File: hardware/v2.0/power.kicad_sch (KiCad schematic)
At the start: 60 parts, among them U1 ECP5U-25F-CABGA256, U2 LTC3407AEDD-2_PBF, U3 TLV62569DBV, U4 LP5912-1.8DRV

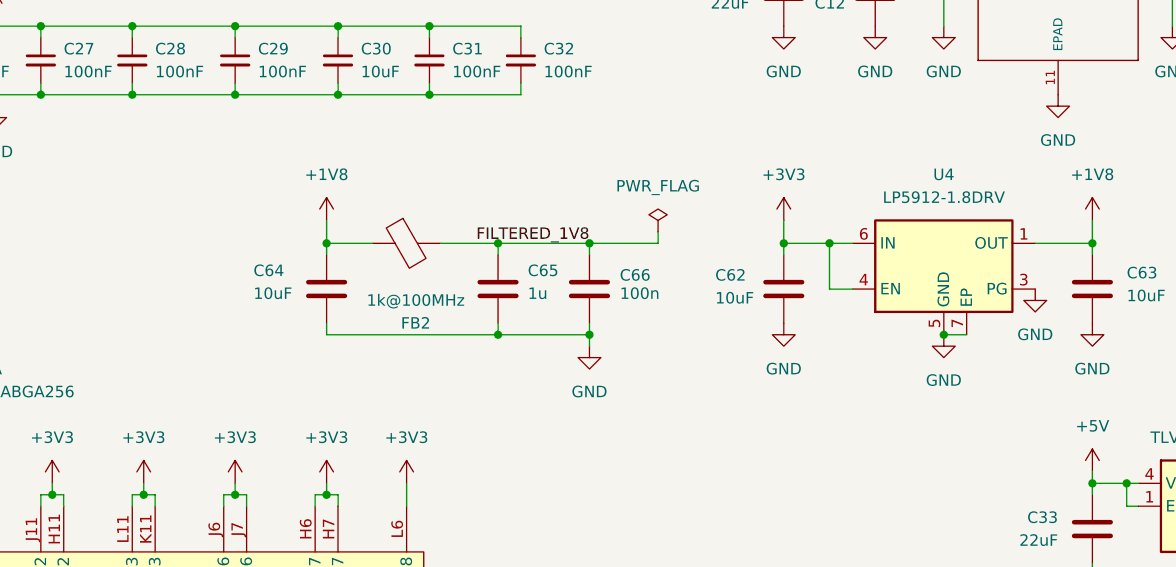
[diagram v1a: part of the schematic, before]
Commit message: ADC driver power and signal input
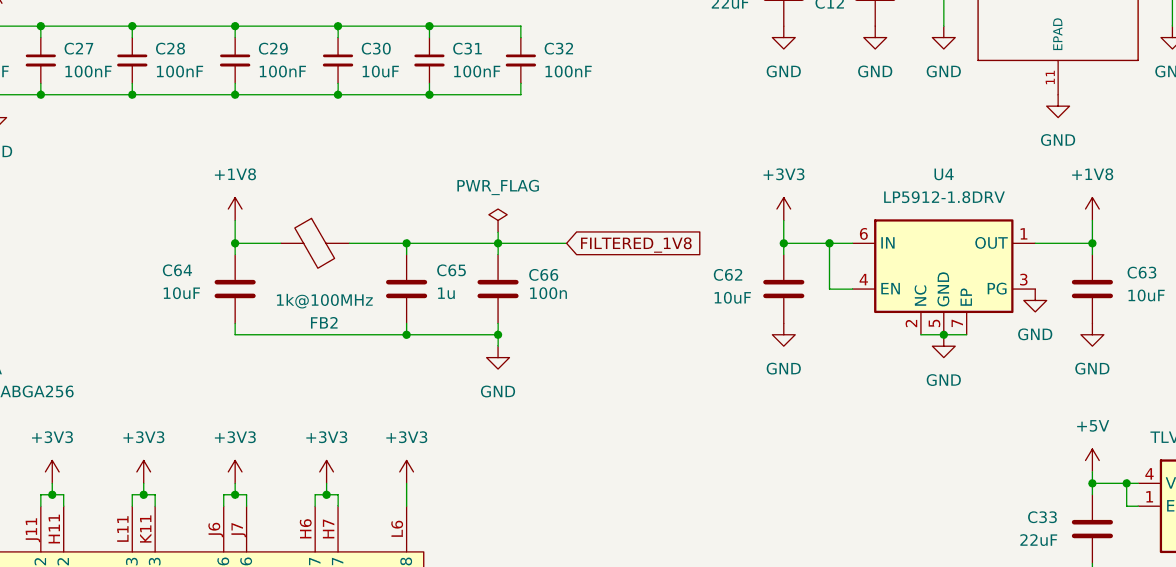
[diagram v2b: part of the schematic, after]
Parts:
- removed U4: LP5912-1.8DRV, Package_SON:WSON-6-1EP_2x2mm_P0.65mm_EP1x1.6mm_ThermalVias, symbol Regulator_Linear:LP5912-1.8DRV
- added U4: LP5912-1.8DRV, Package_SON:WSON-6-1EP_2x2mm_P0.65mm_EP1x1.6mm_ThermalVias, symbol LP5912-1.8DRV:LP5912-1.8DRV
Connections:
- net +1V8: now also U4.1 (OUT)
- net +3V3: now also U4.4 (EN), U4.6 (IN)
- net GND: now also U4.2 (NC), U4.3 (PG), U4.5 (GND), U4.7 (EP)
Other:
- moved on the sheet: C64, C65, C66, FB2

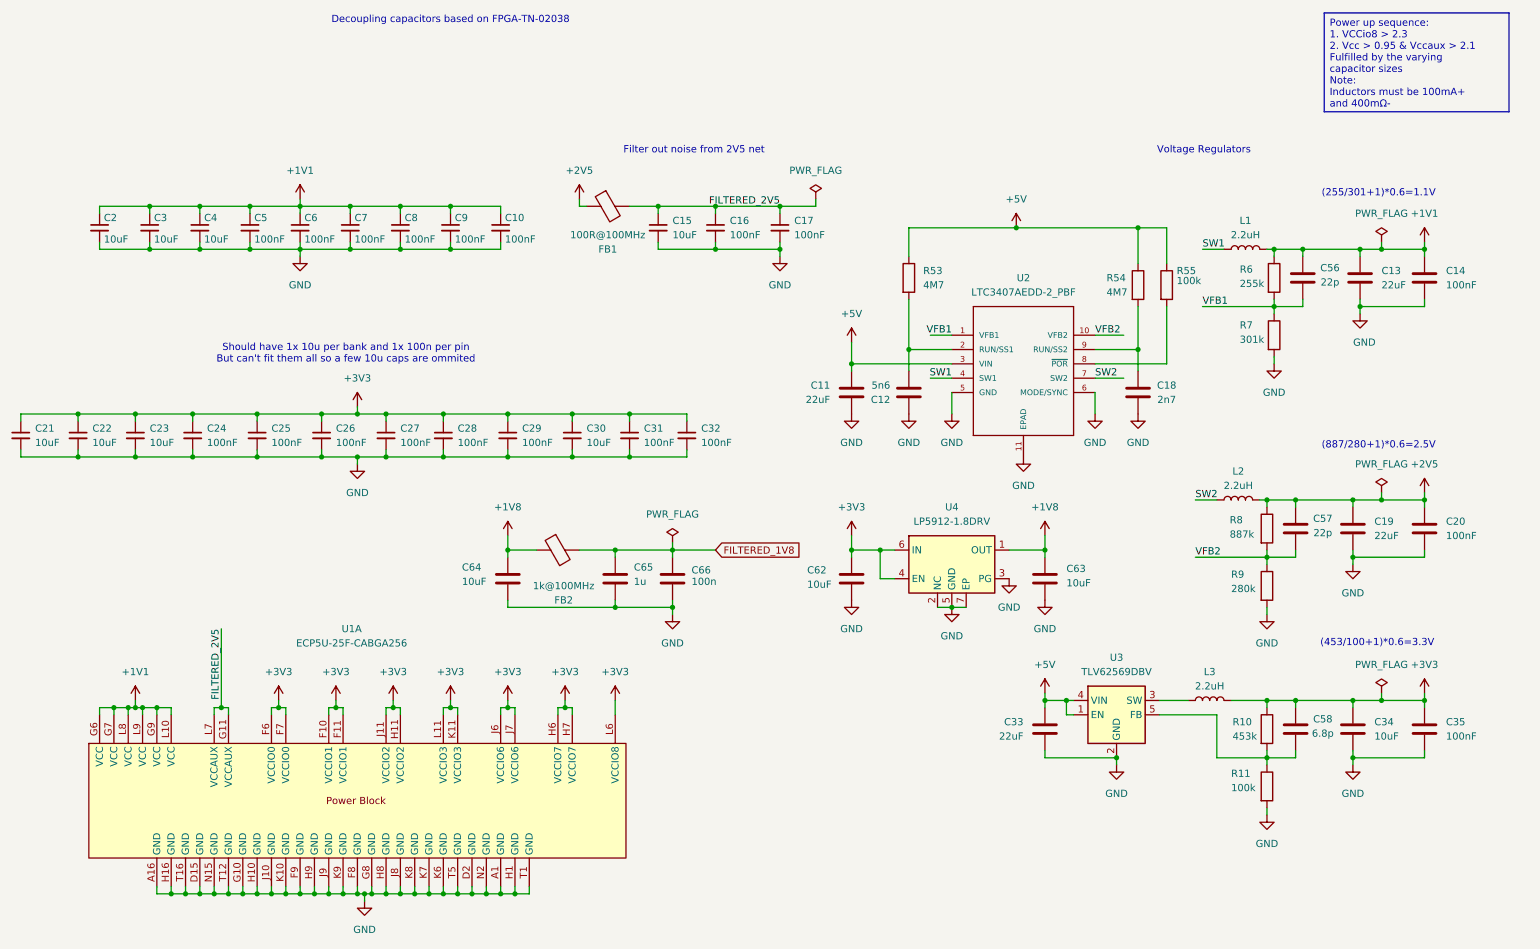
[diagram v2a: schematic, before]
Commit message: BOM fields unification for PCBWay requirements
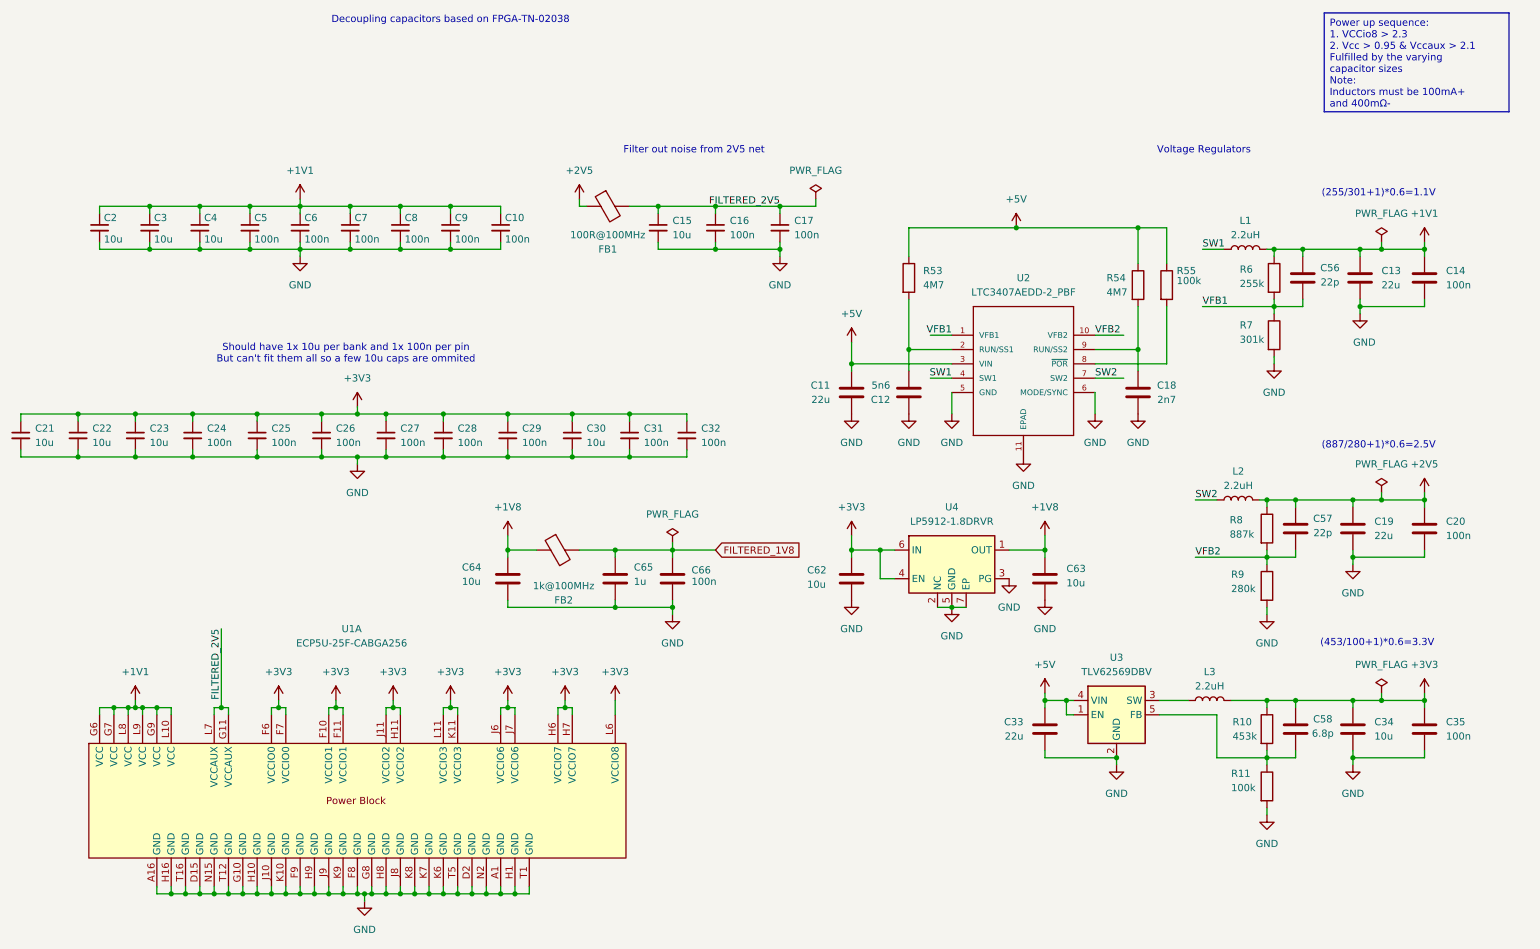
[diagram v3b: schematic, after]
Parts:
- C10, C14, C16, C17, C20, C24, C25, C26, C27, C28, C29, C31, C32, C35, C5, C6, C7, C8, C9: value 100nF -> 100n; MANUFACTURER (none) -> Samsung Electro-Mechanics; MANUFACTURER_PART_NUMBER (none) -> CL05B104KB54PNC
- C11, C13, C19, C33: value 22uF -> 22u; MANUFACTURER (none) -> Samsung Electro-Mechanics; MANUFACTURER_PART_NUMBER (none) -> CL10A226MQ8NRNC
- C12: MANUFACTURER (none) -> Samsung Electro-Mechanics; MANUFACTURER_PART_NUMBER (none) -> CL05B562KB5NNNC
- C15, C2, C21, C22, C23, C3, C30, C34, C4, C62, C63, C64: value 10uF -> 10u; MANUFACTURER (none) -> Samsung Electro-Mechanics; MANUFACTURER_PART_NUMBER (none) -> CL10A106KP8NNNC
- C18: MANUFACTURER (none) -> Samsung Electro-Mechanics; MANUFACTURER_PART_NUMBER (none) -> CL05B272KB5NNNC
- C56, C57: MANUFACTURER (none) -> Samsung Electro-Mechanics; MANUFACTURER_PART_NUMBER (none) -> CL05C220JB5NNNC
- C58: MANUFACTURER (none) -> Samsung Electro-Mechanics; MANUFACTURER_PART_NUMBER (none) -> CL05C6R8CB5NNNC
- C65: MANUFACTURER (none) -> YAGEO; MANUFACTURER_PART_NUMBER (none) -> CC0402KRX5R6BB105
- C66: MANUFACTURER (none) -> Samsung Electro-Mechanics; MANUFACTURER_PART_NUMBER (none) -> CL05B104KB54PNC
- FB1: MANUFACTURER (none) -> FH; MANUFACTURER_PART_NUMBER (none) -> CBG201209U101T
- FB2: MANUFACTURER (none) -> muRata; MANUFACTURER_PART_NUMBER (none) -> BLM18AG102SN1D
- L1, L2, L3: MANUFACTURER (none) -> TDK; MANUFACTURER_PART_NUMBER (none) -> MLP2012S2R2MT0S1
- R10: MANUFACTURER (none) -> UNI-ROYAL; MANUFACTURER_PART_NUMBER (none) -> 0402WGF4533TCE
- R11, R55: MANUFACTURER (none) -> UNI-ROYAL; MANUFACTURER_PART_NUMBER (none) -> 0402WGF1003TCE
- R53, R54: MANUFACTURER (none) -> UNI-ROYAL; MANUFACTURER_PART_NUMBER (none) -> 0402WGF4704TCE
- R6: MANUFACTURER (none) -> UNI-ROYAL; MANUFACTURER_PART_NUMBER (none) -> 0402WGF2553TCE
- R7: MANUFACTURER (none) -> UNI-ROYAL; MANUFACTURER_PART_NUMBER (none) -> 0402WGF3013TCE
- R8: MANUFACTURER (none) -> UNI-ROYAL; MANUFACTURER_PART_NUMBER (none) -> 0402WGF8873TCE
- R9: MANUFACTURER (none) -> UNI-ROYAL; MANUFACTURER_PART_NUMBER (none) -> 0402WGF2803TCE
- U1: MANUFACTURER (none) -> Lattice; MANUFACTURER_PART_NUMBER (none) -> LFE5U-25F-6BG256C
- U2: MANUFACTURER (none) -> ADI; MANUFACTURER_PART_NUMBER ltc3407aedd2 -> LTC3407AEDD-2#PBF
- U3: MANUFACTURER (none) -> TI; MANUFACTURER_PART_NUMBER (none) -> TLV62569DBVR
- U4: value LP5912-1.8DRV -> LP5912-1.8DRVR; MANUFACTURER (none) -> TI; MANUFACTURER_PART_NUMBER (none) -> LP5912-1.8DRVR

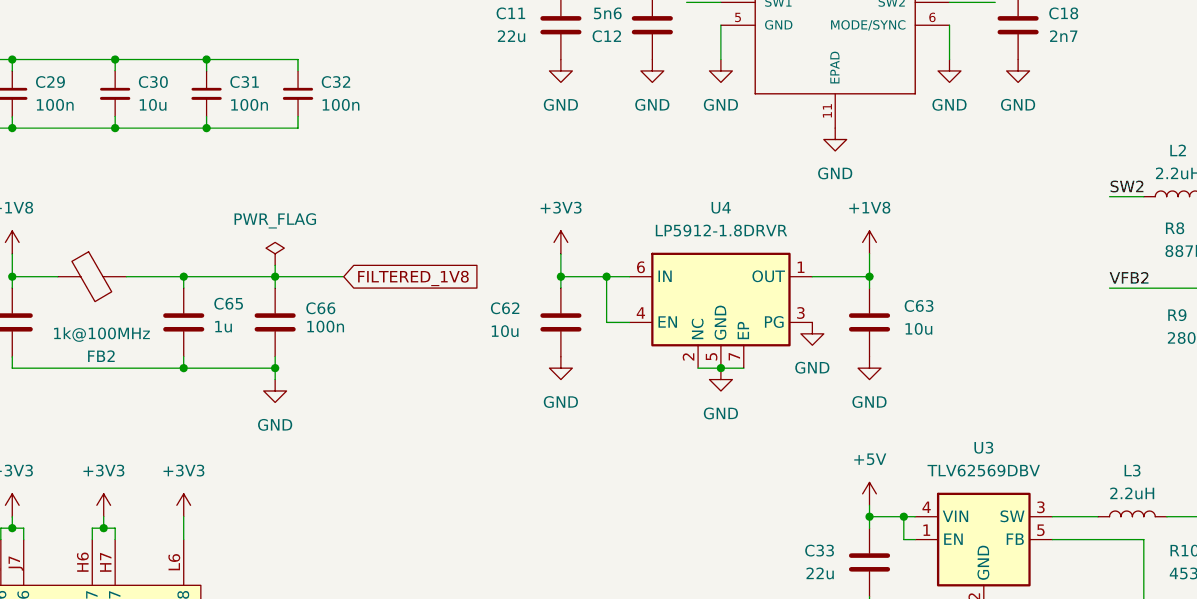
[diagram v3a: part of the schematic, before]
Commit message: ADC datasheet compliance
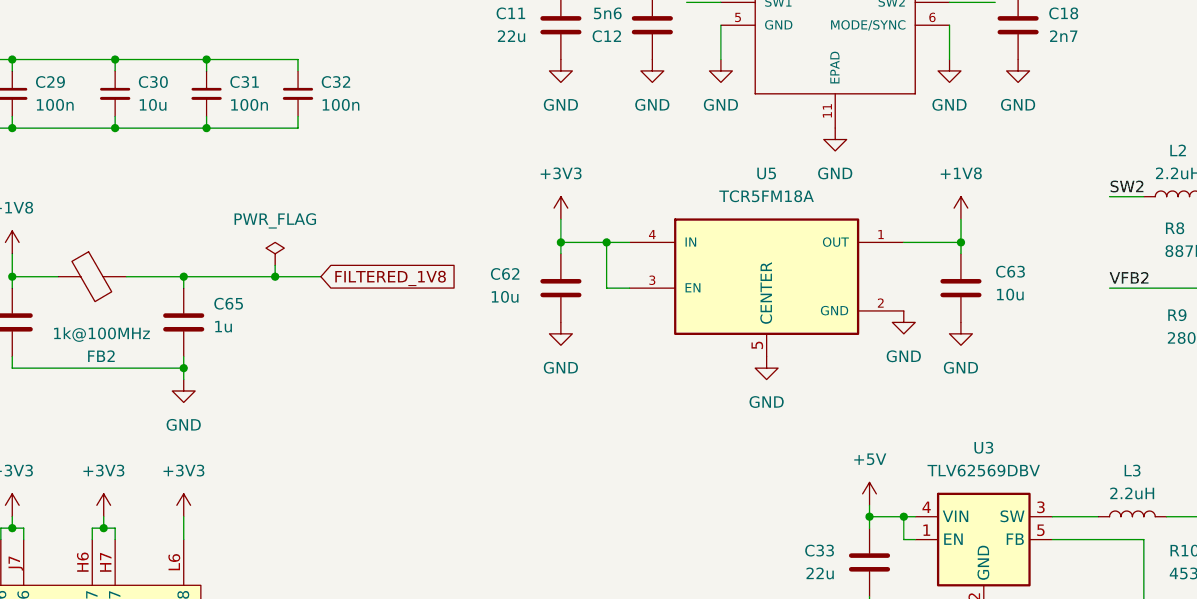
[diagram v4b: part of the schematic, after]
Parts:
- removed C66: 100n, Capacitor_SMD:C_0402_1005Metric, symbol Device:C
- removed U4: LP5912-1.8DRVR, Package_SON:WSON-6-1EP_2x2mm_P0.65mm_EP1x1.6mm_ThermalVias, symbol LP5912-1.8DRV:LP5912-1.8DRV
- added U5: TCR5FM18A, TCR5FM50A:TCR5FM50A, symbol TCR5FM18A:TCR5FM18A
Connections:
- net +1V8: now also U5.1 (OUT)
- net +3V3: now also U5.3 (EN), U5.4 (IN)
- net GND: now also U5.2 (GND), U5.5 (CENTER)
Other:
- moved on the sheet: C62, C63

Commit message: ADC driver power pins bypass
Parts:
- U2: MANUFACTURER_PART_NUMBER LTC3407AEDD-2#PBF -> ltc3407aedd2
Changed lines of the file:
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@@
 			)
 		)
-		(property "Description" "Unpolarized capacitor"
+		(property "Description" "Unpolarized capacitor, small symbol"
 			(at 62.23 87.63 0)
 			(effects
@@
 			)
 		)
-		(property "Description" "Unpolarized capacitor"
+		(property "Description" "Unpolarized capacitor, small symbol"
 			(at 143.51 50.8 0)
 			(effects
@@
 			)
 		)
-		(property "Description" "Unpolarized capacitor"
+		(property "Description" "Unpolarized capacitor, small symbol"
 			(at 30.48 87.63 0)
 			(effects
@@
 			)
 		)
-		(property "Description" "Unpolarized capacitor"
+		(property "Description" "Unpolarized capacitor, small symbol"
 			(at 60.96 50.8 0)
 			(effects
@@
 			)
 		)
-		(property "Description" "Unpolarized capacitor"
+		(property "Description" "Unpolarized capacitor, small symbol"
 			(at 73.66 87.63 0)
 			(effects
@@
 			)
 		)
-		(property "Description" "Unpolarized capacitor"
+		(property "Description" "Unpolarized capacitor, small symbol"
 			(at 34.29 50.8 0)
 			(effects
@@
 			)
 		)
-		(property "Description" "Unpolarized capacitor"
+		(property "Description" "Unpolarized capacitor, small symbol"
 			(at 138.43 87.63 0)
 			(effects
@@
 			)
 		)
-		(property "Description" "Unpolarized capacitor"
+		(property "Description" "Unpolarized capacitor, small symbol"
 			(at 118.11 87.63 0)
 			(effects
@@
 			)
 		)
-		(property "MANUFACTURER_PART_NUMBER" "LTC3407AEDD-2#PBF"
+		(property "MANUFACTURER_PART_NUMBER" "ltc3407aedd2"
 			(at 181.61 69.85 0)
 			(effects
@@
 			)
 		)
-		(property "Description" "Unpolarized capacitor"
+		(property "Description" "Unpolarized capacitor, small symbol"
 			(at 52.07 50.8 0)
 			(effects
@@
 			)
 		)
-		(property "Description" "Unpolarized capacitor"
+		(property "Description" "Unpolarized capacitor, small symbol"
 			(at 128.27 87.63 0)
 			(effects
@@
 			)
 		)
-		(property "Description" "Unpolarized capacitor"
+		(property "Description" "Unpolarized capacitor, small symbol"
 			(at 20.32 87.63 0)
 			(effects
@@
 			)
 		)
-		(property "Description" "Unpolarized capacitor"
+		(property "Description" "Unpolarized capacitor, small symbol"
 			(at 78.74 50.8 0)
 			(effects
@@
 			)
 		)
-		(property "Description" "Unpolarized capacitor"
+		(property "Description" "Unpolarized capacitor, small symbol"
 			(at 105.41 50.8 0)
 			(effects
@@
 			)
 		)
-		(property "Description" "Unpolarized capacitor"
+		(property "Description" "Unpolarized capacitor, small symbol"
 			(at 43.18 50.8 0)
 			(effects
@@
 			)
 		)
-		(property "Description" "Unpolarized capacitor"
+		(property "Description" "Unpolarized capacitor, small symbol"
 			(at 133.35 50.8 0)
 			(effects
@@
 			)
 		)
-		(property "Description" "Unpolarized capacitor"
+		(property "Description" "Unpolarized capacitor, small symbol"
 			(at 96.52 50.8 0)
 			(effects
@@
 			)
 		)
-		(property "Description" "Unpolarized capacitor"
+		(property "Description" "Unpolarized capacitor, small symbol"
 			(at 95.25 87.63 0)
 			(effects
@@
 			)
 		)
-		(property "Description" "Unpolarized capacitor"
+		(property "Description" "Unpolarized capacitor, small symbol"
 			(at 50.8 87.63 0)
 			(effects
@@
 			)
 		)
-		(property "Description" "Unpolarized capacitor"
+		(property "Description" "Unpolarized capacitor, small symbol"
 			(at 85.09 87.63 0)
 			(effects
@@
 			)
 		)
-		(property "Description" "Unpolarized capacitor"
+		(property "Description" "Unpolarized capacitor, small symbol"
 			(at 87.63 50.8 0)
 			(effects
@@
 			)
 		)
-		(property "Description" "Unpolarized capacitor"
+		(property "Description" "Unpolarized capacitor, small symbol"
 			(at 106.68 87.63 0)
 			(effects
@@
 			)
 		)
-		(property "Description" "Unpolarized capacitor"
+		(property "Description" "Unpolarized capacitor, small symbol"
 			(at 69.85 50.8 0)
 			(effects
@@
 			)
 		)
-		(property "Description" "Unpolarized capacitor"
+		(property "Description" "Unpolarized capacitor, small symbol"
 			(at 154.94 50.8 0)
 			(effects
@@
 			)
 		)
-		(property "Description" "Unpolarized capacitor"
+		(property "Description" "Unpolarized capacitor, small symbol"
 			(at 40.64 87.63 0)
 			(effects

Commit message: Repo links update
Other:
- title: Icepi Zero -> GammaPi Zero
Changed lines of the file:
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@@
 	(paper "A4")
 	(title_block
-		(title "Icepi Zero")
-		(date "2026-01-17")
-		(rev "v2.1")
+		(title "GammaPi Zero")
+		(date "2026-01-25")
+		(rev "v2.3.2")
 		(company "Vadym Vikulin, Chengyin Yao (cheyao)")
-		(comment 1 "https://github.com/vikulin/icepi-zero")
+		(comment 1 "https://github.com/vikulin/gammapi-zero")
 		(comment 2 "License: Solderpad")
 		(comment 9 "OSHWA FR000026")
